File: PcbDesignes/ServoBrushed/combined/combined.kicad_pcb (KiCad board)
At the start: 2 copper layers, 36 x 20 mm, 24 parts, among them M1 Motor_DC, U1 ITR8307, U2 ITR8307, U3 AP2112K-3.3, U4 ATSAMD21G18A-A, U5 TB6612FNG

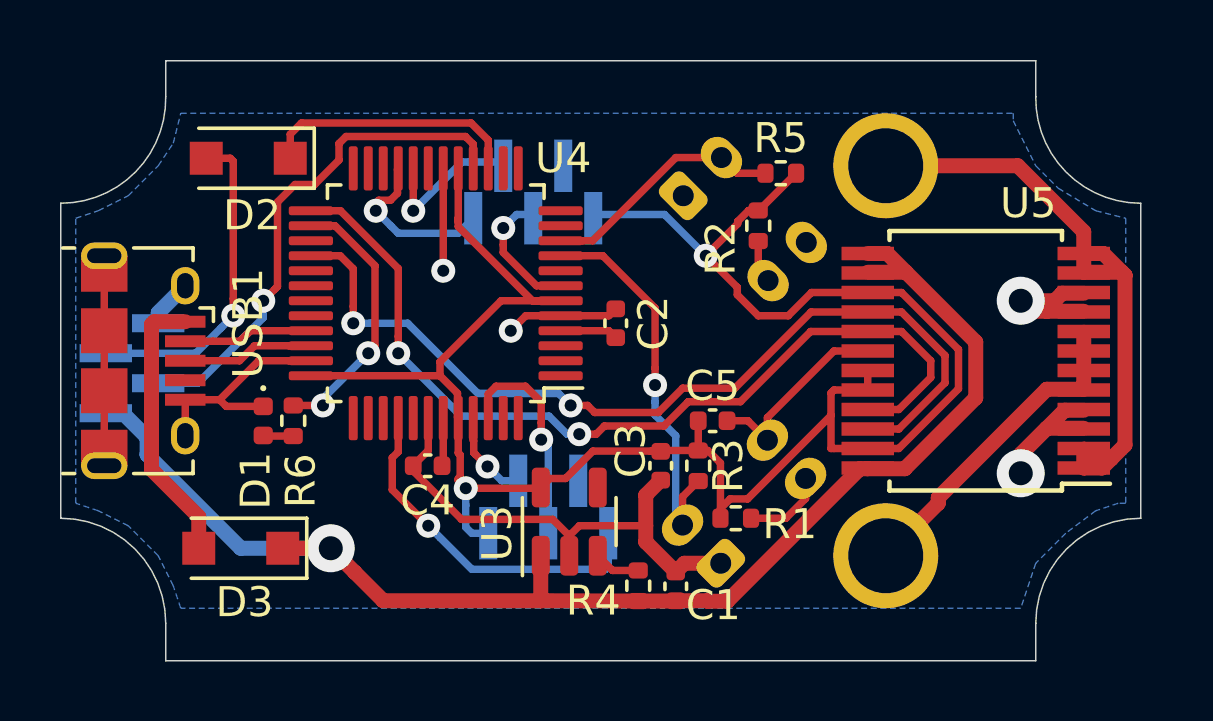
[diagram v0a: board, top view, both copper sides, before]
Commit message: updated version of ServoBrushed combined pcb
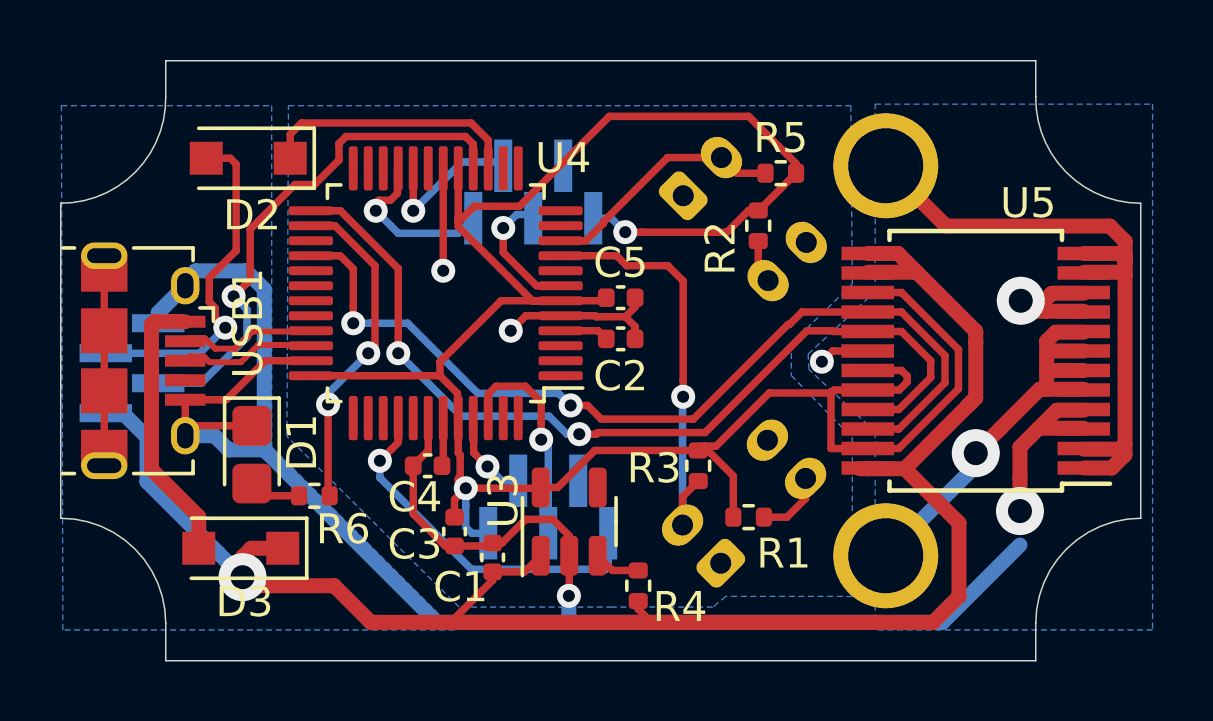
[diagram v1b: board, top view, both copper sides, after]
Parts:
- D1: footprint Diode_SMD:D_0402_1005Metric -> LED_SMD:LED_0805_2012Metric_Castellated
- moved C3 7.21 mm to (90.6, 39.4)
- moved C1 6.18 mm to (91.9, 40.3)
- moved C5 5.12 mm to (96.2, 31.6)
- moved R6 2.60 mm to (86.0, 38.3), turned to 180 degrees
- moved D1 1.19 mm to (83.9, 36.9)
- moved C2 0.55 mm to (96.2, 33.0), turned to 0 degrees
- moved R1 0.43 mm to (100.4, 39.0)
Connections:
- net Net-(U4-Pad33) renamed /USB_D-
- net Net-(U4-Pad34) renamed /USB_D+
- U3 pad 4: (no net) -> Net-(U3-Pad4)
- U4 pad 1: (no net) -> Net-(U4-Pad1)
- U4 pad 11: (no net) -> Net-(U4-Pad11)
- U4 pad 12: (no net) -> Net-(U4-Pad12)
- U4 pad 13: (no net) -> Net-(U4-Pad13)
- U4 pad 14: (no net) -> Net-(U4-Pad14)
- U4 pad 19: (no net) -> Net-(U4-Pad19)
- U4 pad 2: (no net) -> Net-(U4-Pad2)
- U4 pad 22: (no net) -> Net-(U4-Pad22)
- U4 pad 23: (no net) -> Net-(U4-Pad23)
- U4 pad 24: (no net) -> Net-(U4-Pad24)
- U4 pad 27: (no net) -> Net-(U4-Pad27)
- U4 pad 29: (no net) -> Net-(U4-Pad29)
- U4 pad 3: (no net) -> Net-(U4-Pad3)
- U4 pad 30: (no net) -> Net-(U4-Pad30)
- U4 pad 31: (no net) -> Net-(U4-Pad31)
- U4 pad 32: (no net) -> Net-(U4-Pad32)
- U4 pad 37: (no net) -> Net-(U4-Pad37)
- U4 pad 38: (no net) -> Net-(U4-Pad38)
- U4 pad 39: (no net) -> Net-(U4-Pad39)
- U4 pad 41: (no net) -> Net-(U4-Pad41)
- U4 pad 47: (no net) -> Net-(U4-Pad47)
- U4 pad 48: (no net) -> Net-(U4-Pad48)
- U4 pad 8: (no net) -> Net-(U4-Pad8)
- USB1 pad 4: (no net) -> Net-(USB1-Pad4)
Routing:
- net GND: track 55.7 -> 89.8 mm, vias 4 -> 6
- net +BATT: track 46.8 -> 63.5 mm
- net +3V3: track 68.6 -> 79.3 mm
- net Net-(M1-Pad1): track 10.9 -> 14.8 mm, vias 0 -> 1
- net Net-(R6-Pad1): track 9.05 -> 11.0 mm
- net Net-(M1-Pad2): track 21.1 -> 22.2 mm
- net Net-(R3-Pad1): track 13.2 -> 14.3 mm
- net Net-(D1-Pad2): track 1.01 -> 1.74 mm
- net Net-(COM1-Pad2): track 10.9 -> 11.5 mm
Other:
- board text added: "by Adam Bäckström"
- board text removed: "Adamb3.14"

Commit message: Fixed ServoBrushed PCB EMI problem
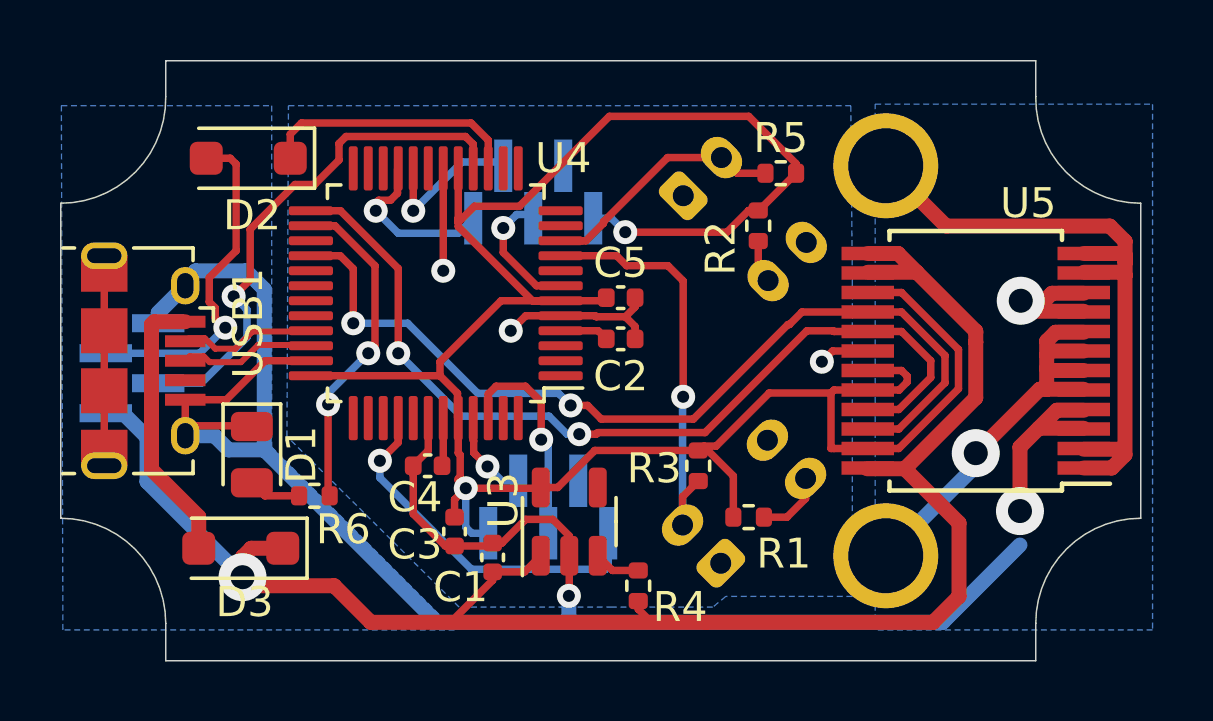
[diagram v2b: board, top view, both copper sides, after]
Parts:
- D1: footprint LED_SMD:LED_0805_2012Metric_Castellated -> LED_SMD:LED_0805_2012Metric
- M1: footprint Connector_Pin:Motor17mm -> Footprints:Motor17mm
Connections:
- net +3V3 renamed +3.3V
- U3 pad 4: Net-(U3-Pad4) -> unconnected-(U3-NC-Pad4)
- U4 pad 1: Net-(U4-Pad1) -> unconnected-(U4-PA00-Pad1)
- U4 pad 11: Net-(U4-Pad11) -> unconnected-(U4-PA06-Pad11)
- U4 pad 12: Net-(U4-Pad12) -> unconnected-(U4-PA07-Pad12)
- U4 pad 13: Net-(U4-Pad13) -> unconnected-(U4-PA08-Pad13)
- U4 pad 14: Net-(U4-Pad14) -> unconnected-(U4-PA09-Pad14)
- U4 pad 19: Net-(U4-Pad19) -> unconnected-(U4-PB10-Pad19)
- U4 pad 2: Net-(U4-Pad2) -> unconnected-(U4-PA01-Pad2)
- U4 pad 22: Net-(U4-Pad22) -> unconnected-(U4-PA13-Pad22)
- U4 pad 23: Net-(U4-Pad23) -> unconnected-(U4-PA14-Pad23)
- U4 pad 24: Net-(U4-Pad24) -> unconnected-(U4-PA15-Pad24)
- U4 pad 27: Net-(U4-Pad27) -> unconnected-(U4-PA18-Pad27)
- U4 pad 29: Net-(U4-Pad29) -> unconnected-(U4-PA20-Pad29)
- U4 pad 3: Net-(U4-Pad3) -> unconnected-(U4-PA02-Pad3)
- U4 pad 30: Net-(U4-Pad30) -> unconnected-(U4-PA21-Pad30)
- U4 pad 31: Net-(U4-Pad31) -> unconnected-(U4-PA22-Pad31)
- U4 pad 32: Net-(U4-Pad32) -> unconnected-(U4-PA23-Pad32)
- U4 pad 37: Net-(U4-Pad37) -> unconnected-(U4-PB22-Pad37)
- U4 pad 38: Net-(U4-Pad38) -> unconnected-(U4-PB23-Pad38)
- U4 pad 39: Net-(U4-Pad39) -> unconnected-(U4-PA27-Pad39)
- U4 pad 41: Net-(U4-Pad41) -> unconnected-(U4-PA28-Pad41)
- U4 pad 47: Net-(U4-Pad47) -> unconnected-(U4-PB02-Pad47)
- U4 pad 48: Net-(U4-Pad48) -> unconnected-(U4-PB03-Pad48)
- U4 pad 8: Net-(U4-Pad8) -> unconnected-(U4-PB09-Pad8)
- USB1 pad 4: Net-(USB1-Pad4) -> unconnected-(USB1-ID-Pad4)
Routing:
- net +BATT: track 63.5 -> 61.7 mm
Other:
- net class Default removed
- net class Power removed
- rule pad_to_mask_clearance: 0.051 -> 0

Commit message: new ServoBrushed PCB
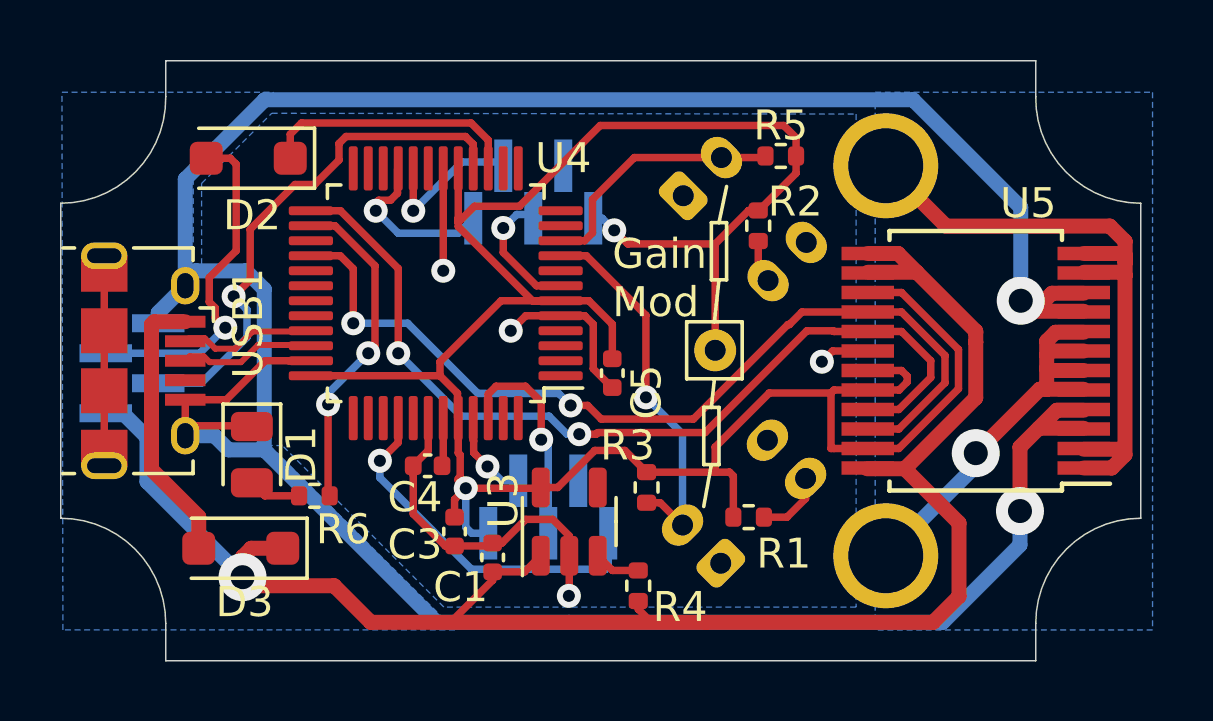
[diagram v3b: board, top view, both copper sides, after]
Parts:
- removed C2: 1uF, Capacitor_SMD:C_0402_1005Metric
- added REF**: Pin_D0.7mm_L6.5mm_W1.8mm_FlatFork, Connector_Pin:Pin_D0.7mm_L6.5mm_W1.8mm_FlatFork, F.Cu at (99.3, 33.4)
- moved C5 2.53 mm to (95.9, 34.2), turned to -90 degrees
- moved R3 1.87 mm to (97.0, 38.0)
- moved R5 0.58 mm to (101.5, 26.9)
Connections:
- U4 pad 4: Net-(U4-PA03) -> unconnected-(U4-PA03-Pad4)
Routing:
- net GND: track 89.5 -> 126.6 mm
- net +3.3V: track 79.0 -> 85.2 mm
- net Net-(U4-PA03): track 1.63 -> 0.00 mm
- net Net-(U1-C): track 14.3 -> 12.7 mm
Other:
- board text added: "Gain Mod"
